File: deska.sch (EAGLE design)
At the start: 15 parts, among them T1 TIP122, T2 TIP122, T3 TIP122

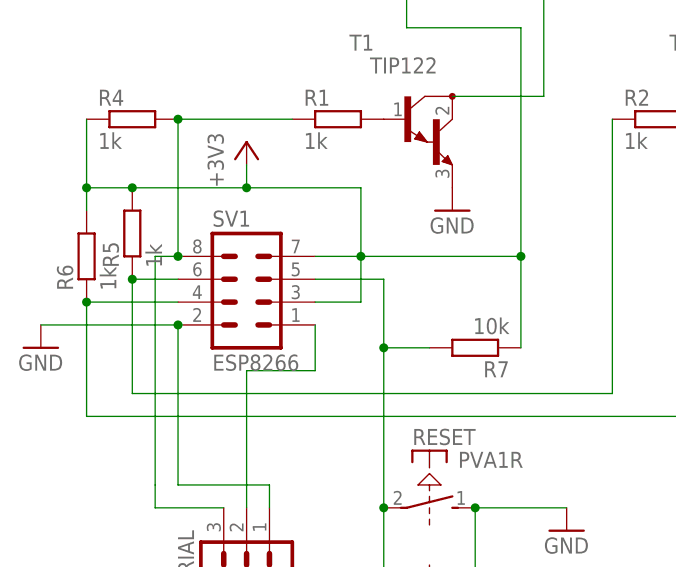
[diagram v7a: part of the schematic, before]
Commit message: upravy desku - popisky
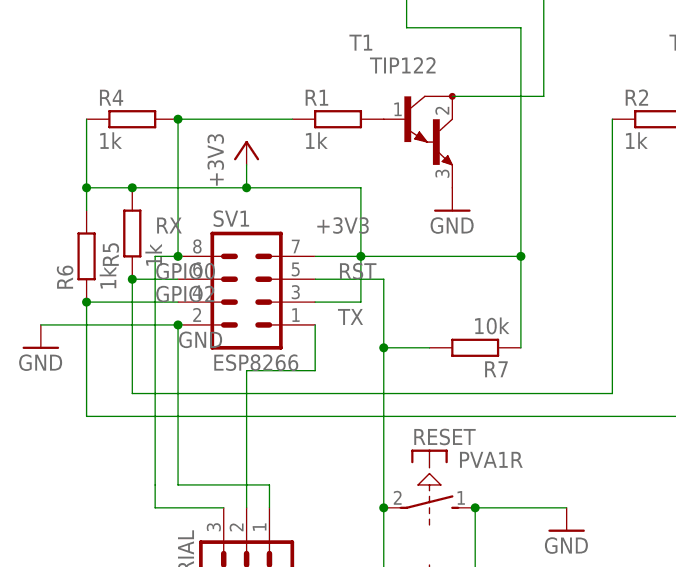
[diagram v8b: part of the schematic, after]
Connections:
- net N$10 renamed GPIO2
- net N$12 renamed RST
- net N$7 renamed RX
- net N$8 renamed GPIO0
- net N$9 renamed TX
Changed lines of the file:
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@@
 <pinref part="SERIAL" gate="G$1" pin="1"/>
 <wire x1="2.54" y1="25.4" x2="2.54" y2="22.86" width="0.1524" layer="91"/>
+<label x="-7.62" y="40.64" size="1.778" layer="95"/>
 </segment>
 <segment>
@@
 </segment>
 </net>
-<net name="N$7" class="0">
+<net name="RX" class="0">
 <segment>
 <pinref part="R1" gate="G$1" pin="1"/>
@@
 <wire x1="-10.16" y1="25.4" x2="-10.16" y2="22.86" width="0.1524" layer="91"/>
 <wire x1="-10.16" y1="22.86" x2="-2.54" y2="22.86" width="0.1524" layer="91"/>
+<label x="-10.16" y="53.34" size="1.778" layer="95"/>
 </segment>
 </net>
-<net name="N$8" class="0">
+<net name="GPIO0" class="0">
 <segment>
 <pinref part="R2" gate="G$1" pin="1"/>
@@
 <pinref part="R5" gate="G$1" pin="1"/>
 <junction x="-12.7" y="48.26"/>
+<label x="-10.16" y="48.26" size="1.778" layer="95"/>
 </segment>
 </net>
-<net name="N$10" class="0">
+<net name="GPIO2" class="0">
 <segment>
 <wire x1="-7.62" y1="45.72" x2="-17.78" y2="45.72" width="0.1524" layer="91"/>
@@
 <pinref part="R6" gate="G$1" pin="1"/>
 <junction x="-17.78" y="45.72"/>
+<label x="-10.16" y="45.72" size="1.778" layer="95"/>
 </segment>
 </net>
-<net name="N$12" class="0">
+<net name="RST" class="0">
 <segment>
 <pinref part="RESET" gate="1" pin="P"/>
@@
 <wire x1="15.24" y1="40.64" x2="20.32" y2="40.64" width="0.1524" layer="91"/>
 <junction x="15.24" y="40.64"/>
+<label x="10.16" y="48.26" size="1.778" layer="95"/>
 </segment>
 </net>
@@
 <wire x1="30.48" y1="76.2" x2="30.48" y2="50.8" width="0.1524" layer="91"/>
 <junction x="30.48" y="50.8"/>
+<label x="7.62" y="53.34" size="1.778" layer="95"/>
 </segment>
 </net>
@@
 </segment>
 </net>
-<net name="N$9" class="0">
+<net name="TX" class="0">
 <segment>
 <pinref part="SV1" gate="G$1" pin="1"/>
@@
 <pinref part="SERIAL" gate="G$1" pin="2"/>
 <wire x1="0" y1="38.1" x2="0" y2="22.86" width="0.1524" layer="91"/>
+<label x="10.16" y="43.18" size="1.778" layer="95"/>
 </segment>
 </net>
